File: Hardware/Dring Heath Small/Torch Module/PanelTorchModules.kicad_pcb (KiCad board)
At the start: 2 copper layers, 137.5 x 130 mm, 196 parts, among them J1 Torch, J10 Module conn, J12 Conn_01x02_Male, J15 Module conn, J2 Module3, J4 Limit, J7 Module1, J8 Torch, J9 2.54 pin, K1 G6E, Q1 IRLML2402, U2 NCV8114ASN150T1G, U3 ADS1115IDGS

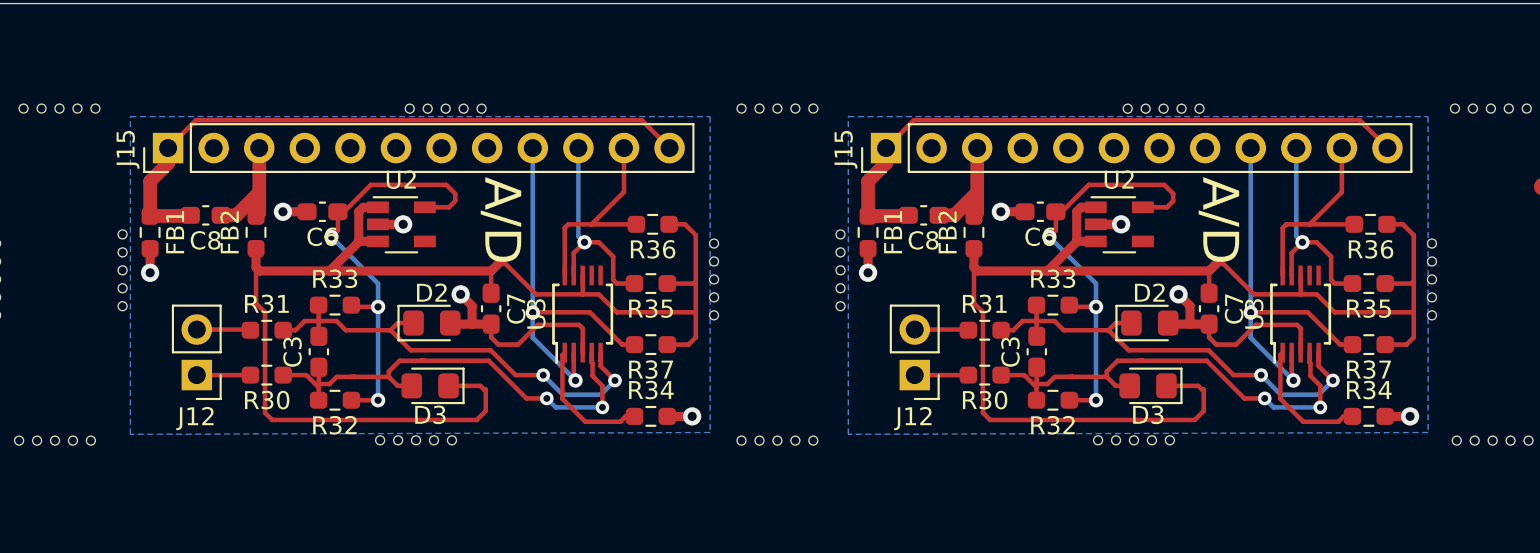
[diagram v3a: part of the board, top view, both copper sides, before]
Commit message: Modified clamped A/D input updates panalized boards
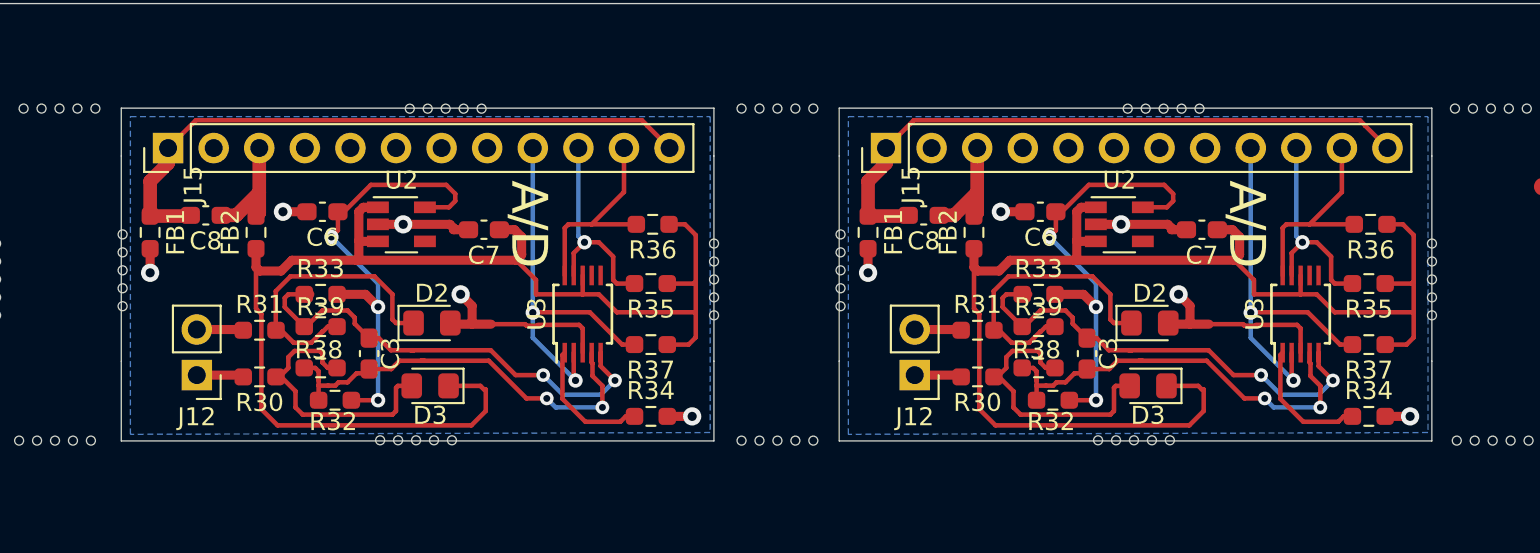
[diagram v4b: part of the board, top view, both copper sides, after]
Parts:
- added R38: 200, Resistor_SMD:R_0603_1608Metric_Pad0.98x0.95mm_HandSolder, F.Cu at (172.3, 52.4)
- added R38: 200, Resistor_SMD:R_0603_1608Metric_Pad0.98x0.95mm_HandSolder, F.Cu at (132.3, 52.4)
- added R39: 200, Resistor_SMD:R_0603_1608Metric_Pad0.98x0.95mm_HandSolder, F.Cu at (172.3, 50.1)
- added R39: 200, Resistor_SMD:R_0603_1608Metric_Pad0.98x0.95mm_HandSolder, F.Cu at (132.3, 50.1)
- C3 (x2): value 100nf -> 22nf
- D2 (x2), D3 (x2): value D_Schottky_Small -> MSCD104H
- R31 (x2): value 1k -> 2k
- moved C7 4.42 mm to (181.4, 44.7), turned to 180 degrees
- moved C7 4.42 mm to (141.4, 44.7), turned to 180 degrees
- moved C3 2.80 mm to (175.0, 51.6)
- moved C3 2.80 mm to (135.0, 51.6)
- moved R33 1.00 mm to (172.3, 48.3)
- moved R33 1.00 mm to (132.3, 48.3)
- moved R30 0.41 mm to (168.9, 52.9)
- moved R30 0.41 mm to (128.9, 52.9)
- moved R31 0.40 mm to (168.9, 50.3)
- moved R31 0.40 mm to (128.9, 50.3)
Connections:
- D2 pad 1: Net-(C3-Pad2) -> Net-(D2-Pad1) (x2)
- D3 pad 2: Net-(C3-Pad1) -> Net-(D3-Pad2) (x2)
- R30 pad 1: Net-(C3-Pad1) -> Net-(D3-Pad2) (x2)
- R31 pad 2: Net-(C3-Pad2) -> Net-(D2-Pad1) (x2)
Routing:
- net Net-(D2-Pad1): track 0.00 -> 32.3 mm
- net Net-(D3-Pad2): track 0.00 -> 30.8 mm
- net Net-(C3-Pad1): track 53.4 -> 48.0 mm
- net Net-(C6-Pad2): track 35.2 -> 40.2 mm
- net Net-(C7-Pad1): track 141.1 -> 143.8 mm
- net Net-(C6-Pad1): track 48.7 -> 50.8 mm
- net Net-(J12-Pad2): track 6.01 -> 5.21 mm
- net Net-(J12-Pad1): track 5.97 -> 5.26 mm
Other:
- outline, holes or cut-outs redrawn

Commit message: removed an edge cut
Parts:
- removed the J15 at (163.8, 40.1)
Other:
- outline, holes or cut-outs redrawn

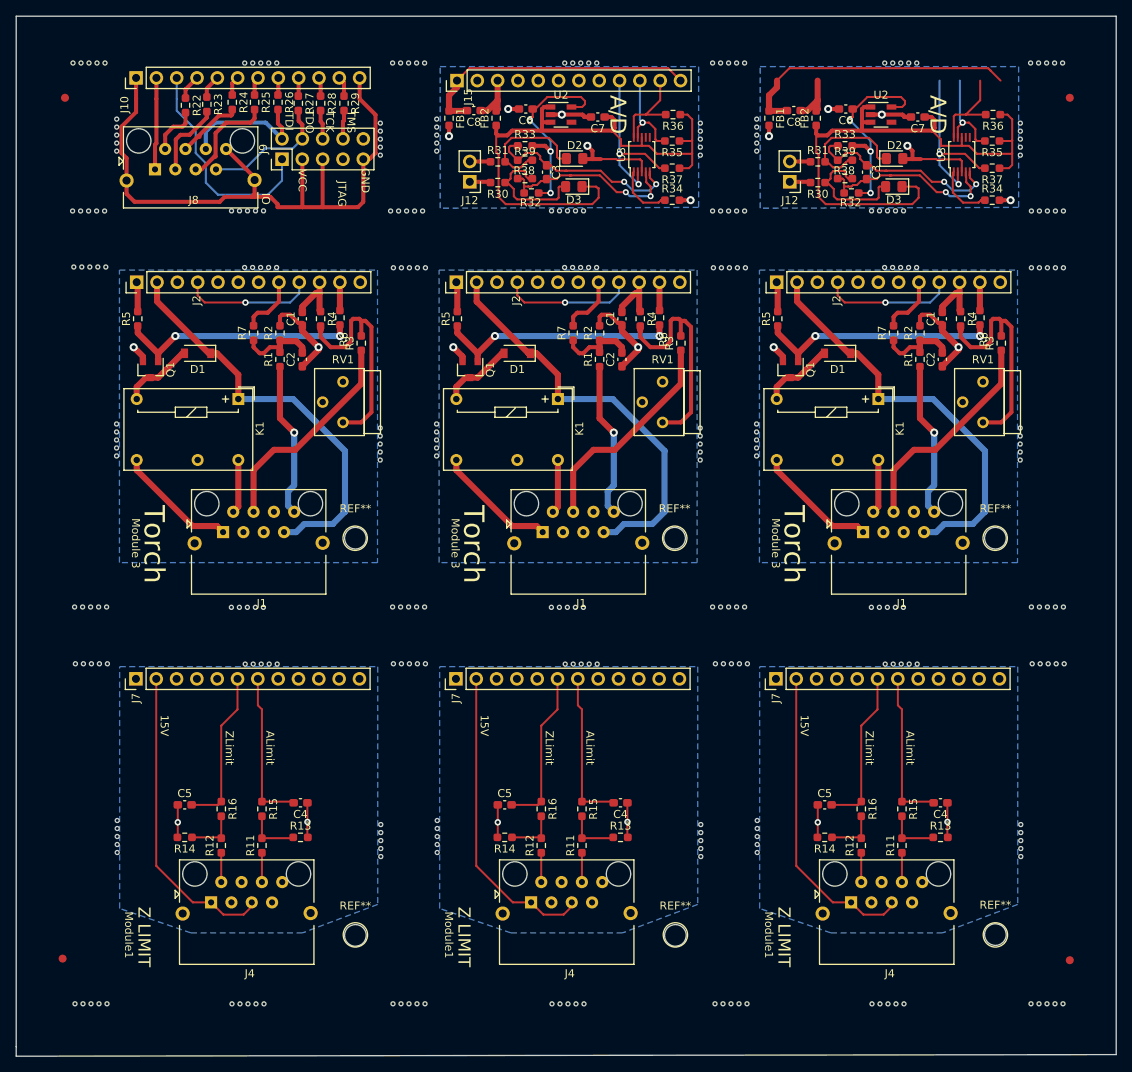
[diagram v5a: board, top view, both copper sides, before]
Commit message: Updated torch module boards for external reset
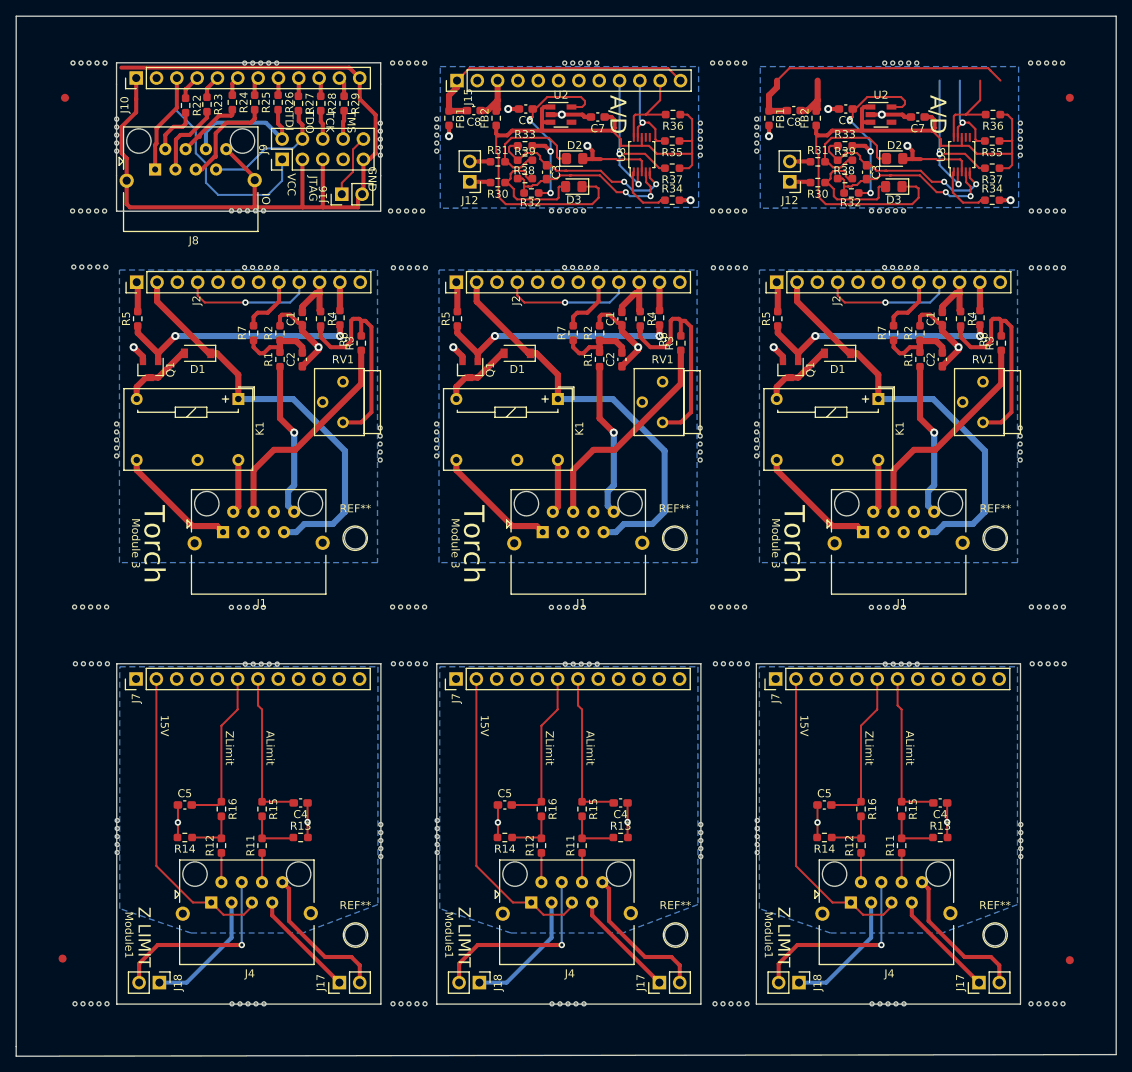
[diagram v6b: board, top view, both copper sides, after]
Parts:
- removed the C4 at (104.2, 130.4)
- removed the C4 at (144.2, 130.4)
- removed the C5 at (89.8, 130.7)
- removed the C5 at (129.8, 130.7)
- removed the J4 at (93.1, 141.9)
- removed the J4 at (133.1, 141.9)
- removed the J7 at (83.7, 114.9)
- removed the J7 at (123.7, 114.9)
- removed the R11 at (99.4, 135.8)
- removed the R11 at (139.4, 135.8)
- removed the R12 at (94.3, 135.8)
- removed the R12 at (134.3, 135.8)
- removed the R13 at (104.2, 134.7)
- removed the R13 at (144.2, 134.7)
- removed the R14 at (89.8, 134.7)
- removed the R14 at (129.8, 134.7)
- removed the R15 at (99.4, 131.2)
- removed the R15 at (139.4, 131.2)
- removed the R16 at (94.3, 131.2)
- removed the R16 at (134.3, 131.2)
- removed the REF** at (151.1, 147.0)
- removed the REF** at (191.1, 146.9)
- added C4: 1uf, Capacitor_SMD:C_0603_1608Metric_Pad1.08x0.95mm_HandSolder, F.Cu at (184.2, 130.4)
- added C4: 1uf, Capacitor_SMD:C_0603_1608Metric_Pad1.08x0.95mm_HandSolder, F.Cu at (144.3, 130.4)
- added C5: 1uf, Capacitor_SMD:C_0603_1608Metric_Pad1.08x0.95mm_HandSolder, F.Cu at (169.7, 130.7)
- added C5: 1uf, Capacitor_SMD:C_0603_1608Metric_Pad1.08x0.95mm_HandSolder, F.Cu at (129.8, 130.7)
- added J16: Reset, Connector_PinHeader_2.54mm:PinHeader_1x02_P2.54mm_Vertical, F.Cu at (109.4, 54.4)
- added J17: Reset, Connector_PinHeader_2.54mm:PinHeader_1x02_P2.54mm_Vertical, F.Cu at (189.1, 152.9)
- added J17: Reset, Connector_PinHeader_2.54mm:PinHeader_1x02_P2.54mm_Vertical, F.Cu at (149.1, 152.9)
- added J17: Reset, Connector_PinHeader_2.54mm:PinHeader_1x02_P2.54mm_Vertical, F.Cu at (109.1, 152.9)
- added J18: Reset, Connector_PinHeader_2.54mm:PinHeader_1x02_P2.54mm_Vertical, F.Cu at (166.6, 152.9)
- added J18: Reset, Connector_PinHeader_2.54mm:PinHeader_1x02_P2.54mm_Vertical, F.Cu at (126.6, 152.9)
- added J18: Reset, Connector_PinHeader_2.54mm:PinHeader_1x02_P2.54mm_Vertical, F.Cu at (86.6, 152.9)
- added J4: Limit, Modules:RJ45_Torb_Vertical, F.Cu at (173.0, 141.9)
- added J4: Limit, Modules:RJ45_Torb_Vertical, F.Cu at (133.1, 141.9)
- added J7: Module1, Connector_PinHeader_2.54mm:PinHeader_1x12_P2.54mm_Vertical, F.Cu at (163.6, 115.0)
- added J7: Module1, Connector_PinHeader_2.54mm:PinHeader_1x12_P2.54mm_Vertical, F.Cu at (123.7, 115.0)
- added R11: 3.3k, Resistor_SMD:R_0603_1608Metric_Pad0.98x0.95mm_HandSolder, F.Cu at (179.4, 135.8)
- added R11: 3.3k, Resistor_SMD:R_0603_1608Metric_Pad0.98x0.95mm_HandSolder, F.Cu at (139.4, 135.8)
- added R12: 3.3k, Resistor_SMD:R_0603_1608Metric_Pad0.98x0.95mm_HandSolder, F.Cu at (174.3, 135.8)
- added R12: 3.3k, Resistor_SMD:R_0603_1608Metric_Pad0.98x0.95mm_HandSolder, F.Cu at (134.3, 135.8)
- added R13: 1k, Resistor_SMD:R_0603_1608Metric_Pad0.98x0.95mm_HandSolder, F.Cu at (184.2, 134.8)
- added R13: 1k, Resistor_SMD:R_0603_1608Metric_Pad0.98x0.95mm_HandSolder, F.Cu at (144.3, 134.8)
- added R14: 1k, Resistor_SMD:R_0603_1608Metric_Pad0.98x0.95mm_HandSolder, F.Cu at (169.7, 134.8)
- added R14: 1k, Resistor_SMD:R_0603_1608Metric_Pad0.98x0.95mm_HandSolder, F.Cu at (129.8, 134.8)
- added R15: 10k, Resistor_SMD:R_0603_1608Metric_Pad0.98x0.95mm_HandSolder, F.Cu at (179.4, 131.2)
- added R15: 10k, Resistor_SMD:R_0603_1608Metric_Pad0.98x0.95mm_HandSolder, F.Cu at (139.4, 131.2)
- added R16: 10k, Resistor_SMD:R_0603_1608Metric_Pad0.98x0.95mm_HandSolder, F.Cu at (174.3, 131.2)
- added R16: 10k, Resistor_SMD:R_0603_1608Metric_Pad0.98x0.95mm_HandSolder, F.Cu at (134.3, 131.2)
- added REF**: MountingHole_2.7mm, MountingHole:MountingHole_2.7mm, F.Cu at (191.1, 146.9)
- added REF**: MountingHole_2.7mm, MountingHole:MountingHole_2.7mm, F.Cu at (151.1, 146.9)
- moved C4 80.0 mm to (104.3, 130.4)
- moved R11 80.0 mm to (99.4, 135.8)
- moved R12 80.0 mm to (94.3, 135.8)
- moved R13 80.0 mm to (104.3, 134.8)
- moved R15 80.0 mm to (99.4, 131.2)
- moved R16 80.0 mm to (94.3, 131.2)
- moved C5 80.0 mm to (89.8, 130.7)
- moved J4 80.0 mm to (93.1, 141.9)
- moved J7 80.0 mm to (83.7, 115.0)
- moved R14 80.0 mm to (89.8, 134.8)
- moved REF** 0.05 mm to (111.1, 146.9)
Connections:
- J8 pad 1: Net-(J10-Pad2) -> Net-(J10-Pad3)
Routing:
- net Net-(J18-Pad2): track 0.00 -> 72.1 mm, vias 0 -> 3
- net Net-(J17-Pad2): track 0.00 -> 55.5 mm
- net Net-(J18-Pad1): track 0.00 -> 47.2 mm
- net Net-(J17-Pad1): track 0.00 -> 40.5 mm
- net Net-(J10-Pad1): track 83.8 -> 115.4 mm
- net Net-(J10-Pad3): track 28.1 -> 40.7 mm
- net Net-(J10-Pad2): track 11.5 -> 0.00 mm
- net Net-(J16-Pad1): track 0.00 -> 8.02 mm
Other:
- outline, holes or cut-outs redrawn
